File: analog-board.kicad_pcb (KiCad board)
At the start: 2 copper layers, 200 x 150 mm, 481 parts, among them J1 AC IN, J2 OUT, J3 CONN_20X2, P2 CONN_01X02, Q1 2N3906, Q10 2N3906, Q11 2N3906, Q12 2N3906, Q13 2N3906, Q14 2N3906, Q15 2N3906, Q16 2N3906, Q17 NPN, Q18 NPN, Q19 J111, Q2 2N3906, Q20 2N3906, Q3 2N3906, Q4 2N3906, Q5 2N3906, Q6 BCM857BS, Q7 2N3906, Q8 2N3906, Q9 2N3906, U1 LM13700, U10 ADR01, U11 DG212B, U12 DG212B, U13 DG408, U14 DG408, U15 TL072-, U16 DG408, U17 DG408, U18 LM13700, U19 LM13700, U2 LM13700, U21 TL072-, U22 TL074-, U23 TL074-, U24 TL074-, U25 TL074-, U26 TL072-, U27 TL074-, U28 TL074-, U29 LM13700, U3 LM13700, U30 LM13700, U31 TL074-, U32 LM13700, U33 TL074-, U34 TL074-, U35 TL074-, U36 74LV573, U38 0 - 10V, U39 TL074-, U4 DG212B, U40 DG419, U41 0 - 10V, U42 10 - 0V, U43 LM7812, U44 LM7912, U45 DG408, U46 7805, U5 TL074-, U6 AD5556, U7 TL072-, U8 TL074-, U9 AD8672

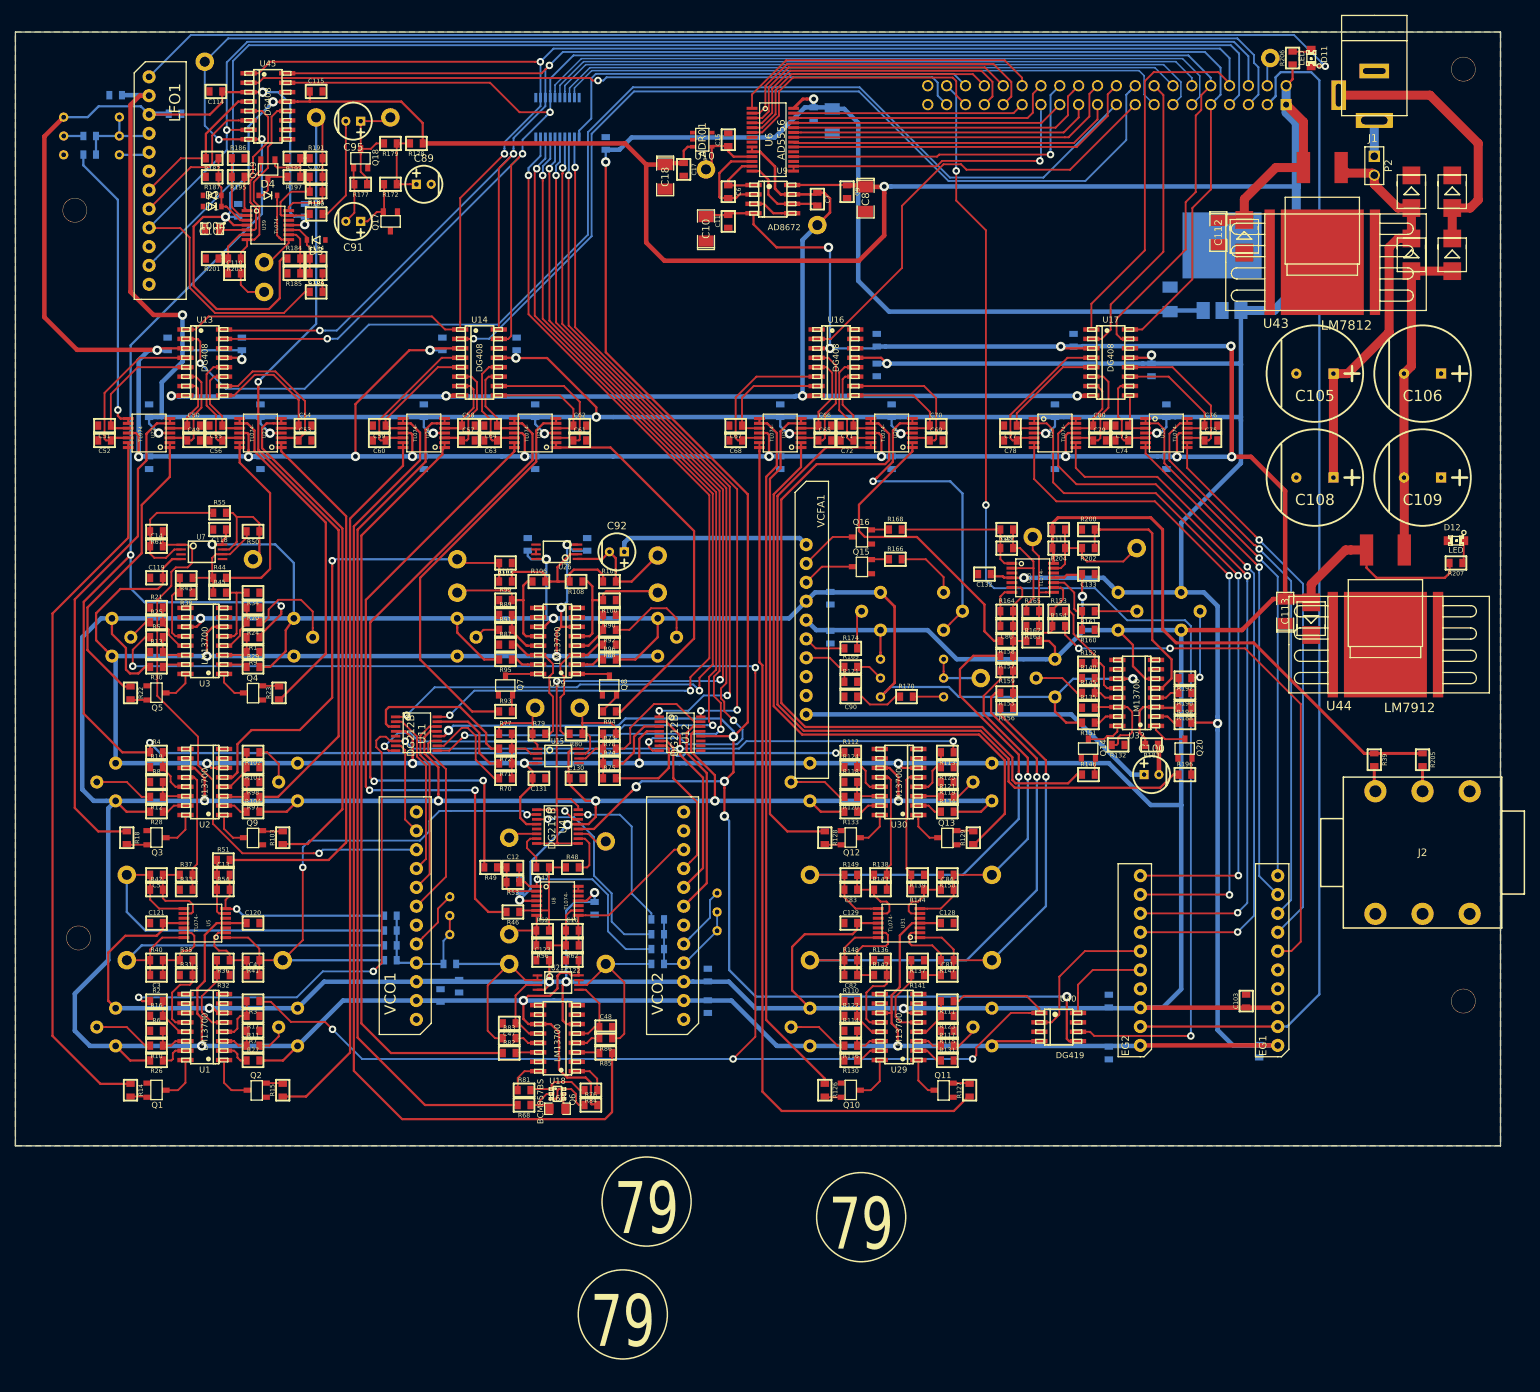
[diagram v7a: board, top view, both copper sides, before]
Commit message: all power and signal traces routed, need to connect outstanding grounds and fix a few routing misconnects
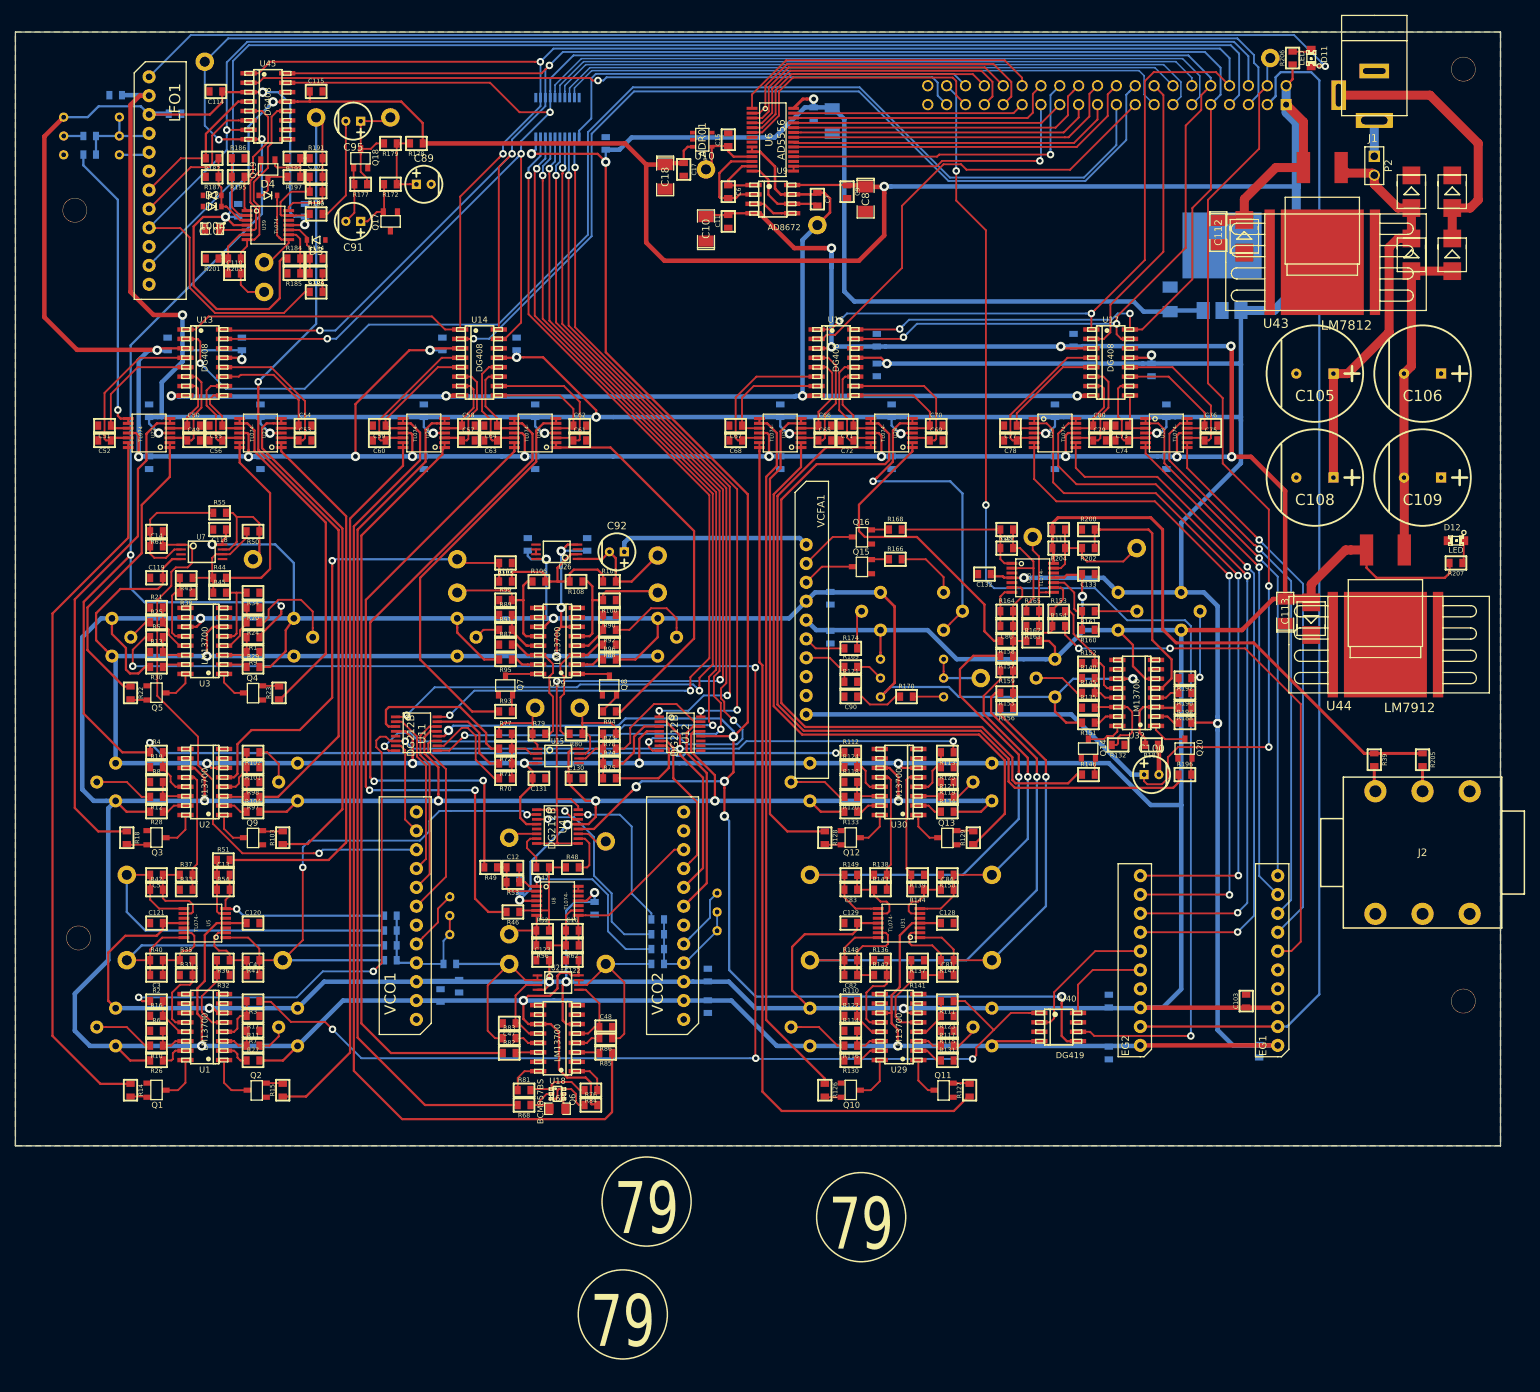
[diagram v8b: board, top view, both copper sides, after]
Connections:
- C53 pad 1: SH6 -> SH4
- C54 pad 1: SH7 -> SH5
- C55 pad 1: SH5 -> SH7
- C56 pad 1: SH4 -> SH6
- U23 pad 10: SH5 -> SH7
- U23 pad 12: SH4 -> SH6
- U23 pad 3: SH6 -> SH4
- U23 pad 5: SH7 -> SH5
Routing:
- net TUNE: track 52.8 -> 170.1 mm, vias 0 -> 2
- net DB1: track 256.3 -> 296.2 mm, vias 3 -> 5
- net DB0: track 266.0 -> 303.7 mm, vias 2 -> 4
- net DB2: track 259.6 -> 295.2 mm, vias 3 -> 5
- net +5V: track 354.6 -> 368.4 mm, vias 8 -> 9
- net SH7: track 18.6 -> 8.87 mm
- net SH6: track 21.5 -> 13.0 mm
- net EG2: track 267.7 -> 260.3 mm
- net SH5: track 11.4 -> 17.5 mm
- net SH4: track 15.4 -> 21.3 mm
- net DAC MUX EN0: track 163.9 -> 167.1 mm
- net -12V: track 1225.7 -> 1228.4 mm
- net Net-(R101-Pad2): track 6.37 -> 8.28 mm
- net Net-(EG2-Pad6): track 20.6 -> 19.6 mm
- net VOL CV: track 105.2 -> 105.8 mm
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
